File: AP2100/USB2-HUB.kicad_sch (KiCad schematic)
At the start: 10 parts, among them U4 TPD4EUSB30, U7 AP22653W6

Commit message: Finish PoE section Rename CM4IO library as AP2100
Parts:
- U4: symbol CM4IO:TPD4EUSB30 -> AP2100:TPD4EUSB30
- U7: symbol CM4IO:AP2553W6 -> AP2100:AP2553W6
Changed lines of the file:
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@@
   (junction (at 224.155 70.485) (diameter 1.016) (color 0 0 0 0))
   (junction (at 234.315 70.485) (diameter 1.016) (color 0 0 0 0))
-  (no_connect (at 73.66 54.61))
   (no_connect (at 94.615 90.805))
   (no_connect (at 73.66 59.69))
+  (no_connect (at 73.66 54.61))
   (wire (pts (xy 84.455 106.045) (xy 86.995 106.045))
     (stroke (width 0) (type solid) (color 0 0 0 0))
@@
   (symbol (lib_id "power:GND") (at 86.995 107.315 0) (unit 1)
     (in_bom yes) (on_board yes)
-    (property "Reference" "#PWR?" (id 0) (at 86.995 113.665 0)
+    (property "Reference" "#PWR0101" (id 0) (at 86.995 113.665 0)
       (effects (font (size 1.27 1.27)) hide)
     )
@@
     )
   )
-  (symbol (lib_id "CM4IO:AP2553W6") (at 173.355 73.025 0) (unit 1)
+  (symbol (lib_id "AP2100:AP2553W6") (at 173.355 73.025 0) (unit 1)
     (in_bom yes) (on_board yes)
     (property "Reference" "U7" (id 0) (at 172.72 63.754 0))
@@
     )
   )
-  (symbol (lib_id "CM4IO:TPD4EUSB30") (at 86.36 57.15 0) (unit 1)
+  (symbol (lib_id "AP2100:TPD4EUSB30") (at 86.36 57.15 0) (unit 1)
     (in_bom yes) (on_board yes)
     (property "Reference" "U4" (id 0) (at 86.36 45.2882 0))

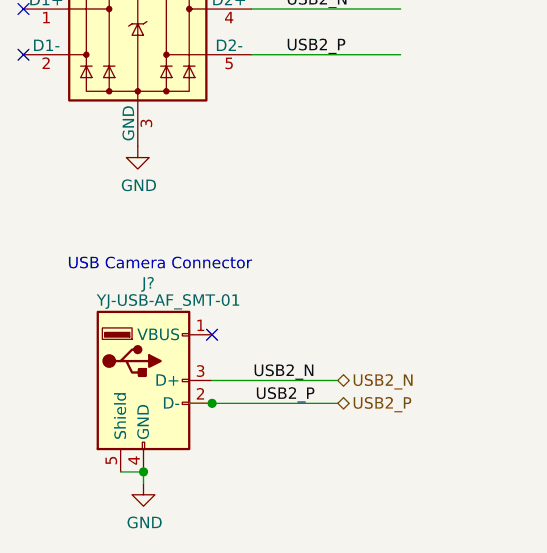
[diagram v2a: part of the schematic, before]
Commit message: Add AP3000 single radio for security cameras. Add CM4IO Raspi board
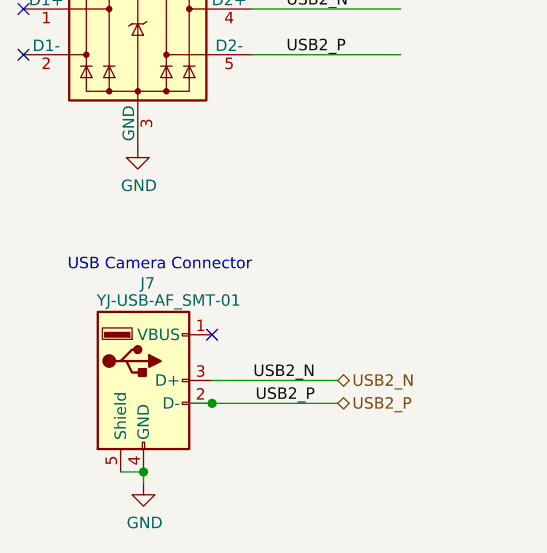
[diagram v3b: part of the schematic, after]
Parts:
- gave numbers to parts that had none: 1
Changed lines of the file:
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@@
   (junction (at 224.155 70.485) (diameter 1.016) (color 0 0 0 0))
   (junction (at 234.315 70.485) (diameter 1.016) (color 0 0 0 0))
+  (no_connect (at 94.615 90.805))
   (no_connect (at 73.66 54.61))
-  (no_connect (at 94.615 90.805))
   (no_connect (at 73.66 59.69))
   (wire (pts (xy 84.455 106.045) (xy 86.995 106.045))
@@
   (symbol (lib_id "Scott:YJ-USB-AF_SMT-01") (at 86.995 95.885 0) (unit 1)
     (in_bom yes) (on_board yes)
-    (property "Reference" "J?" (id 0) (at 88.265 85.09 0)
+    (property "Reference" "J7" (id 0) (at 88.265 85.09 0)
       (effects (font (size 1.27 1.27)) (justify right))
     )
